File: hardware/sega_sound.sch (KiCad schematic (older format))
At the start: 3 parts

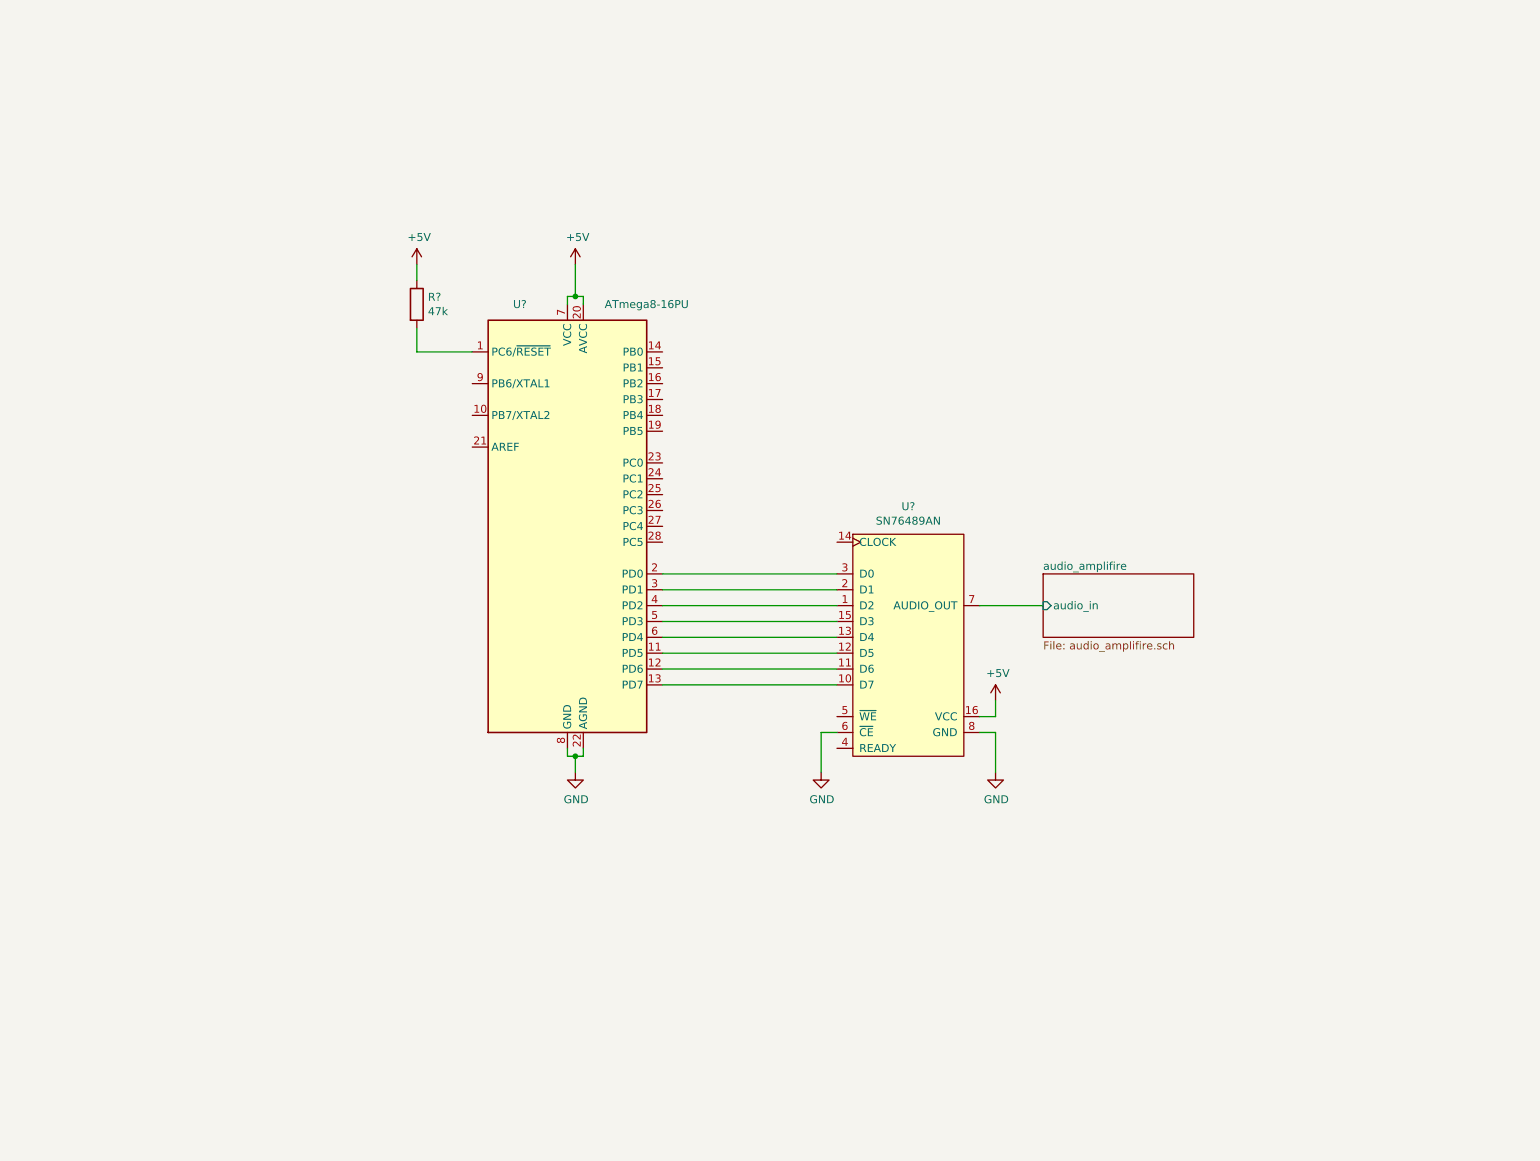
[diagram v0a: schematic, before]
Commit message: changed schematic
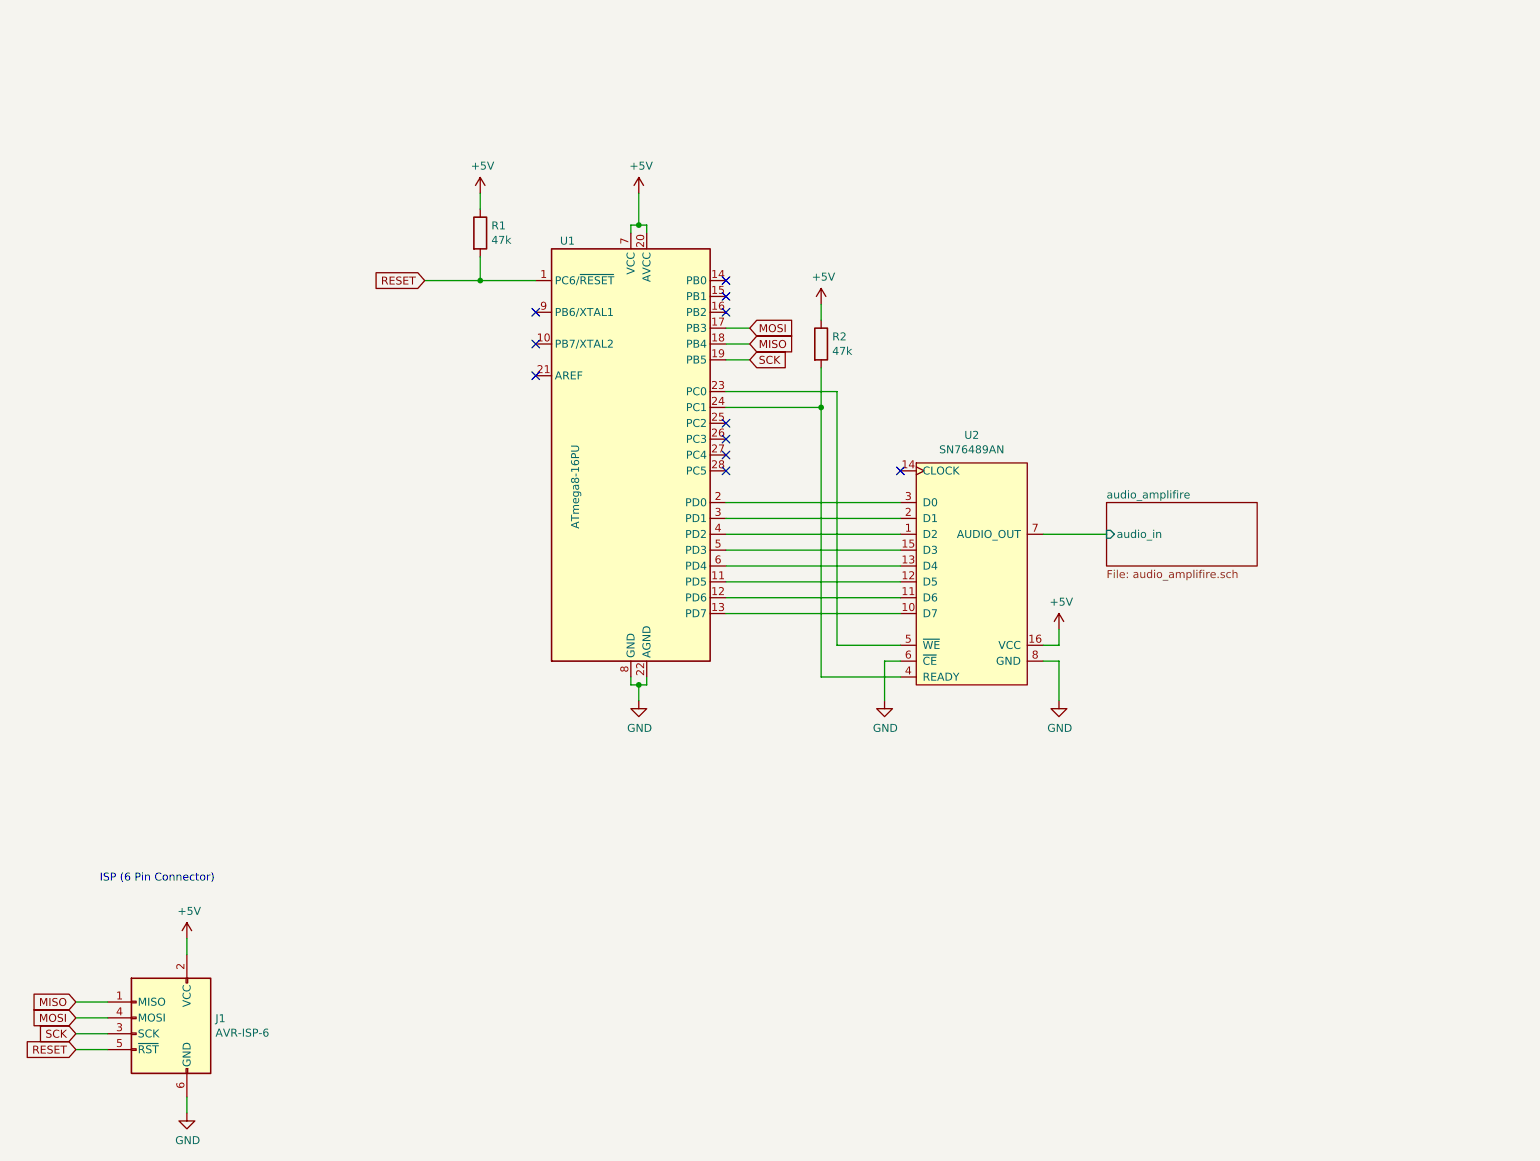
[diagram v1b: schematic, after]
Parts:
- removed U?: ATmega8-16PU, Package_DIP:DIP-28_W7.62mm, symbol MCU_Microchip_ATmega:ATmega8-16PU
- added J1: AVR-ISP-6, symbol Connector:AVR-ISP-6
- added R2: 47k, symbol Device:R
- added U1: ATmega8-16PU, Package_DIP:DIP-28_W7.62mm, symbol MCU_Microchip_ATmega:ATmega8-16PU
- gave numbers to parts that had none: 2
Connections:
- net +5V: now also J1.2 (VCC), R2.1, U1.20 (AVCC), U1.7 (VCC)
- net GND: now also J1.6 (GND), U1.22 (AGND), U1.8 (GND)
- net RESET: now reaches R1.2
- net RESET: now also J1.5 (~RST), U1.1 (PC6/~RESET)
- net at U2.12 (D5): now also U1.11 (PD5)
- net at U2.11 (D6): now also U1.12 (PD6)
- net at U2.10 (D7): now also U1.13 (PD7)
- net at U2.3 (D0): now also U1.2 (PD0)
- net at U2.2 (D1): now also U1.3 (PD1)
- net at U2.1 (D2): now also U1.4 (PD2)
- net at U2.15 (D3): now also U1.5 (PD3)
- net at U2.13 (D4): now also U1.6 (PD4)
- net at U2.4 (READY): now also R2.2, U1.24 (PC1)
- net at U2.5 (~WE): now also U1.23 (PC0)
- new net MISO: J1.1 (MISO), U1.18 (PB4)
- new net MOSI: J1.4 (MOSI), U1.17 (PB3)
- new net SCK: J1.3 (SCK), U1.19 (PB5)
- no-connect marks 0 -> 11
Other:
- note added: "ISP (6 Pin Connector)"
- moved on the sheet: R1, U2

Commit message: removed pullup resistor 47k for READY signal
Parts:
- removed R2: 47k, symbol Device:R
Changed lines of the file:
@@
 $EndDescr
 $Comp
-L power:+5V #PWR04
+L power:+5V #PWR03
 U 1 1 5E271210
 P 7250 4400
-F 0 "#PWR04" H 7250 4250 50  0001 C CNN
+F 0 "#PWR03" H 7250 4250 50  0001 C CNN
 F 1 "+5V" H 7265 4573 50  0000 C CNN
 F 2 "" H 7250 4400 50  0001 C CNN
@@
 Connection ~ 4600 1850
 $Comp
-L power:GND #PWR05
+L power:GND #PWR04
 U 1 1 5E273378
 P 4600 4850
-F 0 "#PWR05" H 4600 4600 50  0001 C CNN
+F 0 "#PWR04" H 4600 4600 50  0001 C CNN
 F 1 "GND" H 4605 4677 50  0000 C CNN
 F 2 "" H 4600 4850 50  0001 C CNN
@@
 Connection ~ 4600 4750
 $Comp
-L power:GND #PWR07
+L power:GND #PWR06
 U 1 1 5E2743A8
 P 7250 4850
-F 0 "#PWR07" H 7250 4600 50  0001 C CNN
+F 0 "#PWR06" H 7250 4600 50  0001 C CNN
 F 1 "GND" H 7255 4677 50  0000 C CNN
 F 2 "" H 7250 4850 50  0001 C CNN
@@
 	7250 4600 7250 4850
 $Comp
-L power:GND #PWR06
+L power:GND #PWR05
 U 1 1 5E275910
 P 6150 4850
-F 0 "#PWR06" H 6150 4600 50  0001 C CNN
+F 0 "#PWR05" H 6150 4600 50  0001 C CNN
 F 1 "GND" H 6155 4677 50  0000 C CNN
 F 2 "" H 6150 4850 50  0001 C CNN
@@
 Connection ~ 3600 2200
 $Comp
-L power:+5V #PWR08
+L power:+5V #PWR07
 U 1 1 5E279685
 P 1750 6350
-F 0 "#PWR08" H 1750 6200 50  0001 C CNN
+F 0 "#PWR07" H 1750 6200 50  0001 C CNN
 F 1 "+5V" H 1765 6523 50  0000 C CNN
 F 2 "" H 1750 6350 50  0001 C CNN
@@
 $EndComp
 $Comp
-L power:GND #PWR09
+L power:GND #PWR08
 U 1 1 5E279E4E
 P 1750 7450
-F 0 "#PWR09" H 1750 7200 50  0001 C CNN
+F 0 "#PWR08" H 1750 7200 50  0001 C CNN
 F 1 "GND" H 1755 7277 50  0000 C CNN
 F 2 "" H 1750 7450 50  0001 C CNN
@@
 NoConn ~ 3950 2400
 NoConn ~ 6250 3400
-$Comp
-L Device:R R2
-U 1 1 5E294E27
-P 5750 2600
-F 0 "R2" H 5820 2646 50  0000 L CNN
-F 1 "47k" H 5820 2555 50  0000 L CNN
-F 2 "" V 5680 2600 50  0001 C CNN
-F 3 "~" H 5750 2600 50  0001 C CNN
-	1    5750 2600
-	1    0    0    -1
-$EndComp
-Wire Wire Line
-	5750 2750 5750 3000
-Connection ~ 5750 3000
-$Comp
-L power:+5V #PWR03
-U 1 1 5E299157
-P 5750 2350
-F 0 "#PWR03" H 5750 2200 50  0001 C CNN
-F 1 "+5V" H 5765 2523 50  0000 C CNN
-F 2 "" H 5750 2350 50  0001 C CNN
-F 3 "" H 5750 2350 50  0001 C CNN
-	1    5750 2350
-	1    0    0    -1
-$EndComp
-Wire Wire Line
-	5750 2350 5750 2450
 $EndSCHEMATC

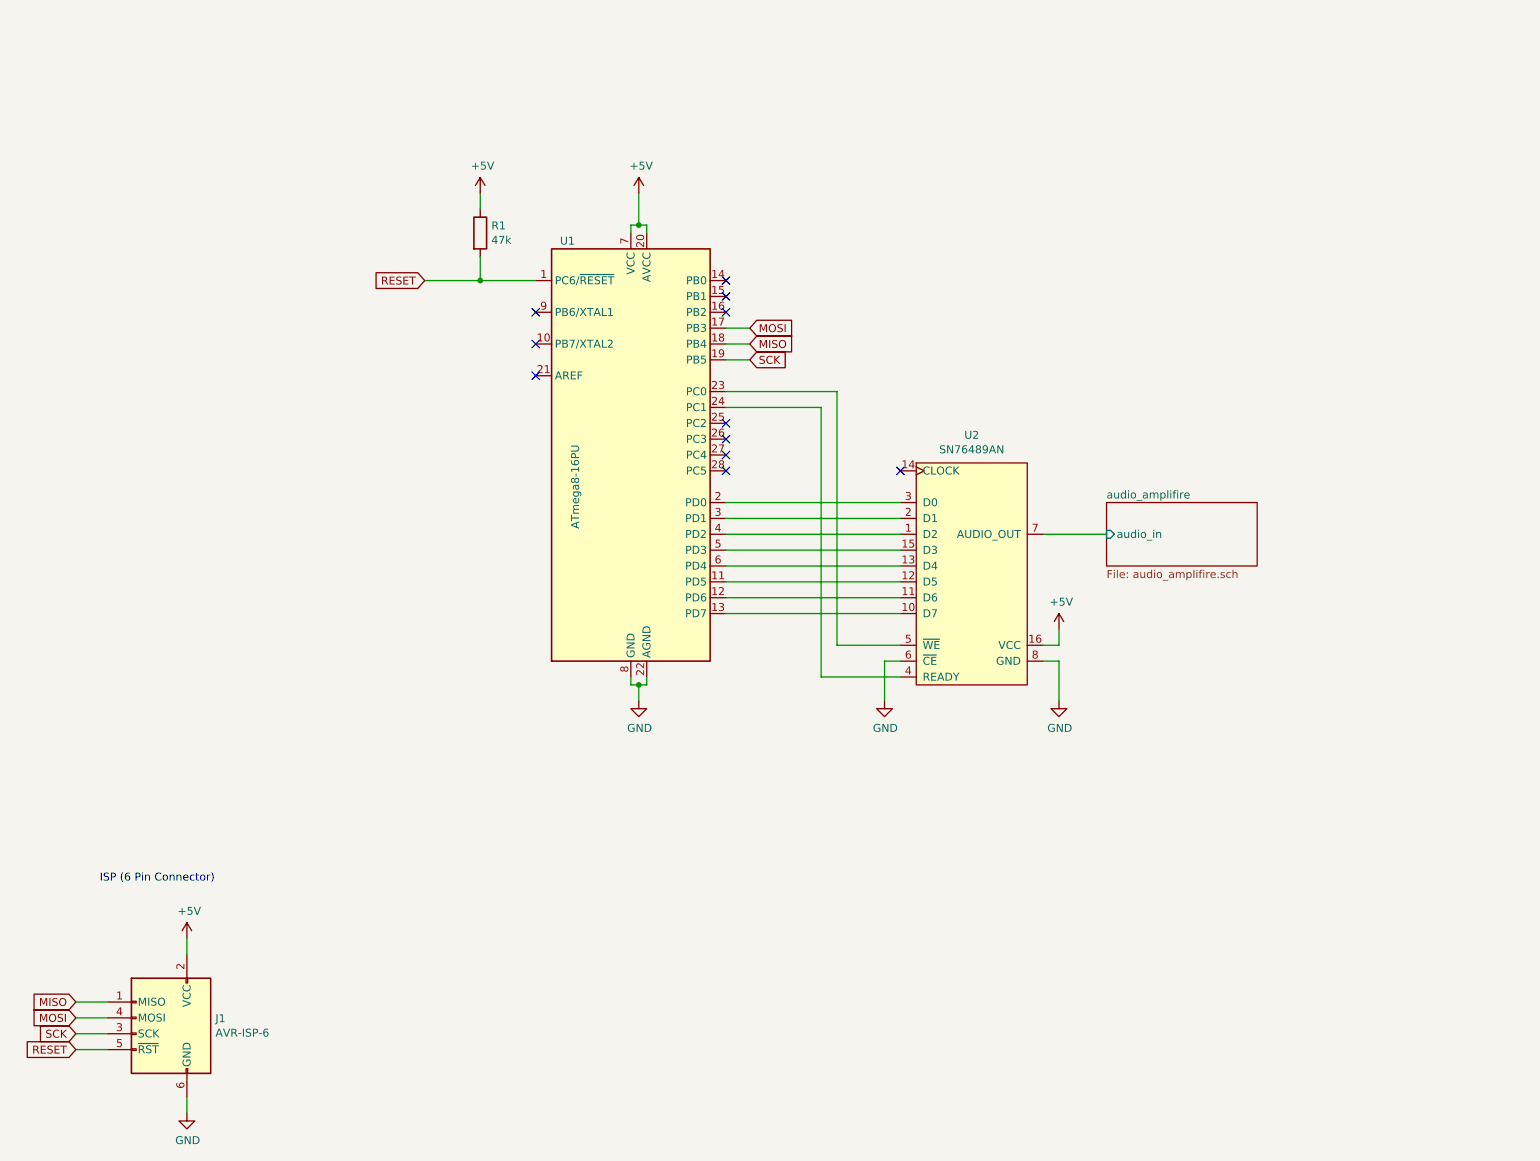
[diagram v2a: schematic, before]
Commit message: changed schematic
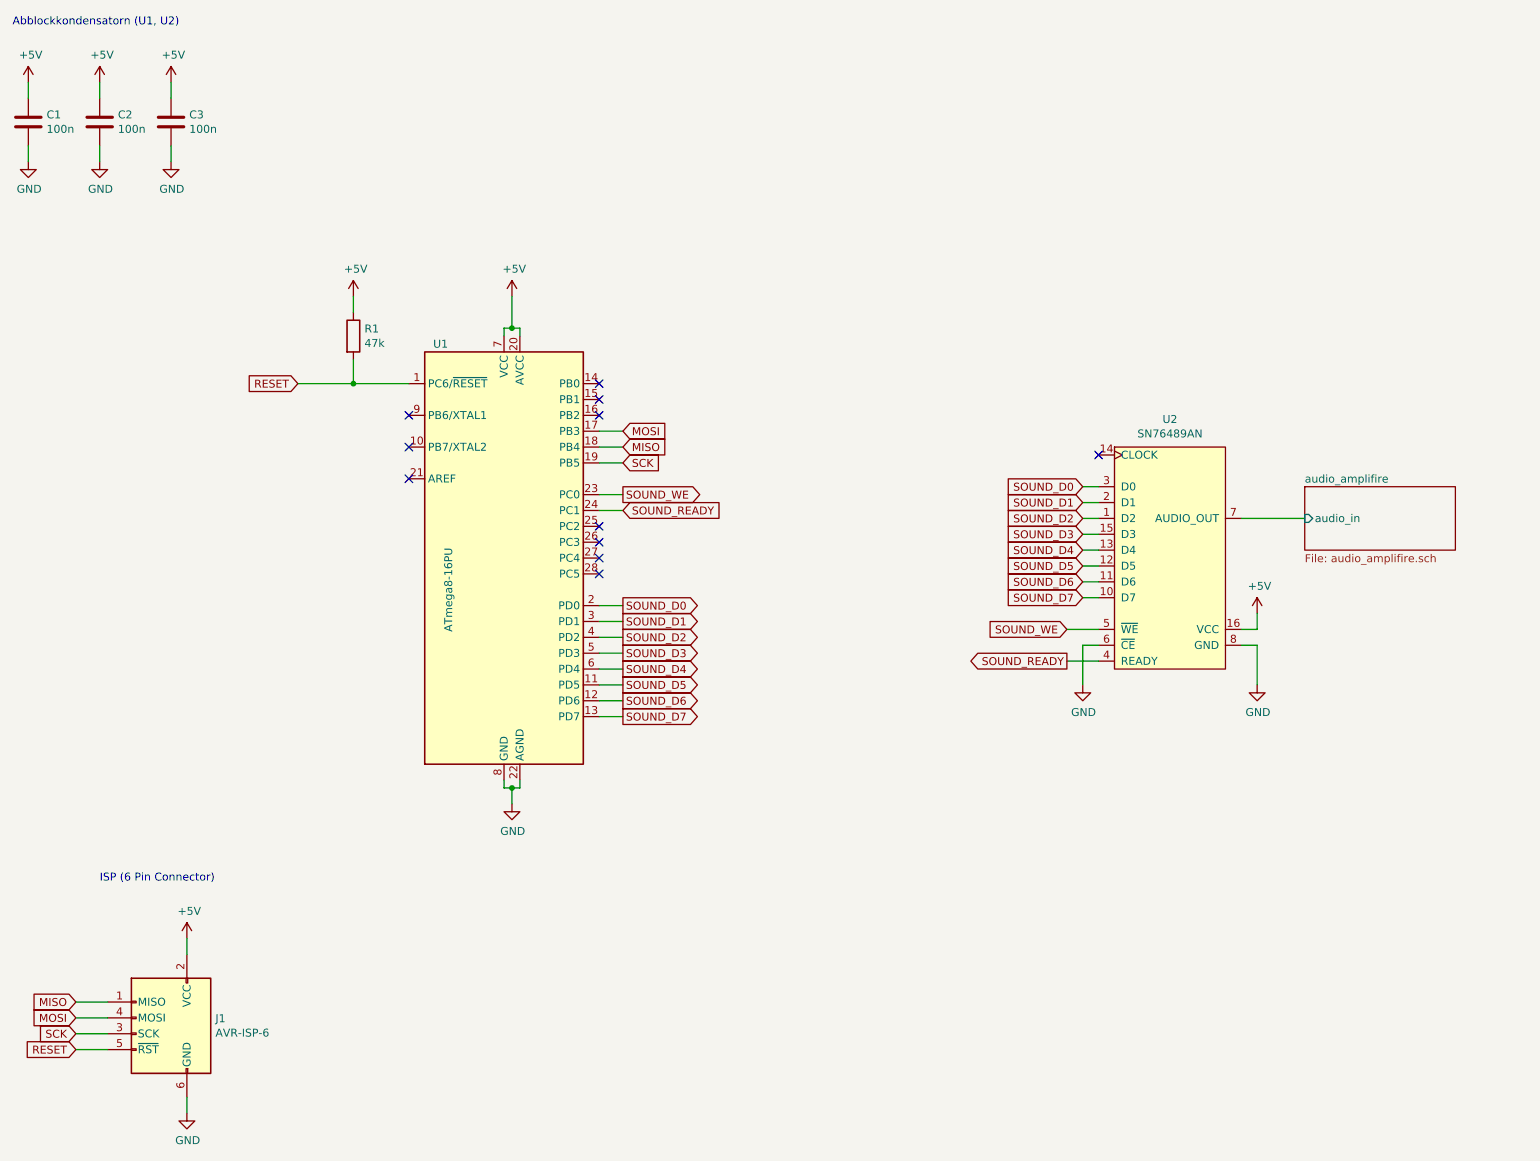
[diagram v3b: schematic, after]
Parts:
- added C1, C2, C3: 100n, symbol Device:C
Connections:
- net +5V: now also C1.1, C2.1, C3.1
- net GND: now also C1.2, C2.2, C3.2
- net SOUND_D2: now reaches U1.4 (PD2), U2.1 (D2)
- net SOUND_D7: now reaches U1.13 (PD7), U2.10 (D7)
- net SOUND_D6: now reaches U1.12 (PD6), U2.11 (D6)
- net SOUND_D5: now reaches U1.11 (PD5), U2.12 (D5)
- net SOUND_D4: now reaches U1.6 (PD4), U2.13 (D4)
- net SOUND_D3: now reaches U1.5 (PD3), U2.15 (D3)
- net SOUND_D1: now reaches U1.3 (PD1), U2.2 (D1)
- net SOUND_D0: now reaches U1.2 (PD0), U2.3 (D0)
- net SOUND_READY: now reaches U1.24 (PC1), U2.4 (READY)
- net SOUND_WE: now reaches U1.23 (PC0), U2.5 (~WE)
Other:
- note added: "Abblockkondensatorn (U1, U2)"
- moved on the sheet: R1, U1

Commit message: added status led in schematic
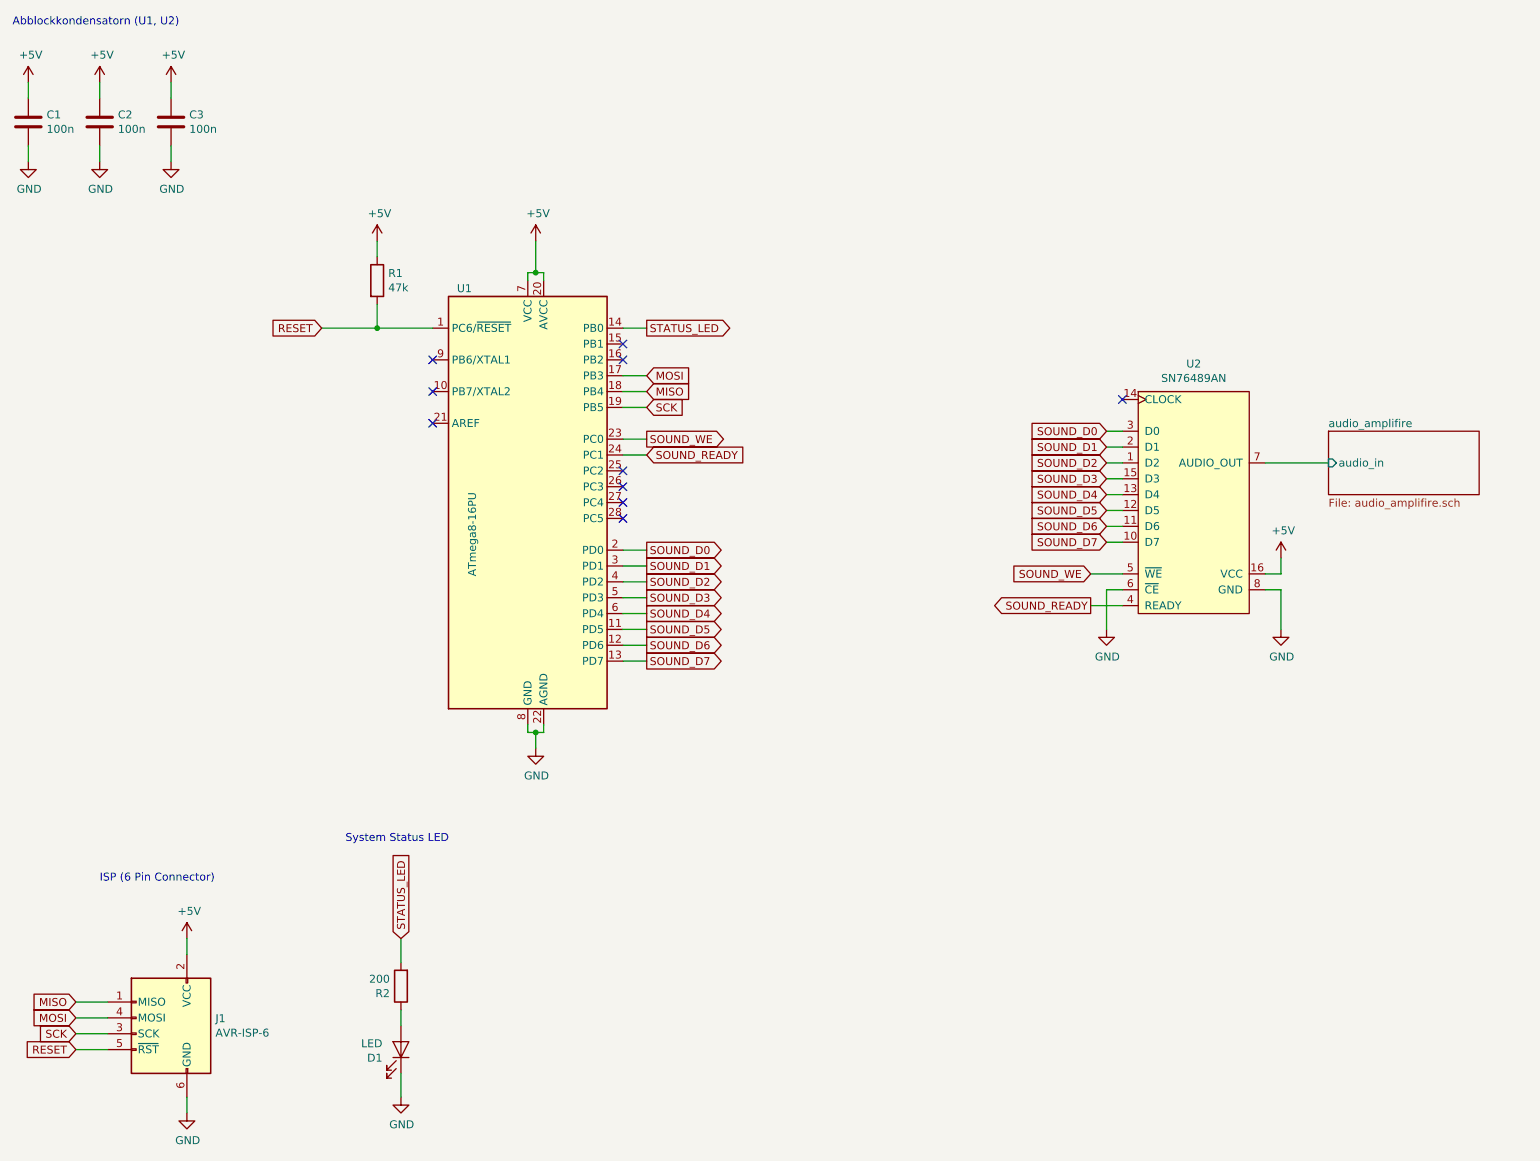
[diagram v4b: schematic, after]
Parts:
- added D1: LED, symbol Device:LED
- added R2: 200, symbol Device:R
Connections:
- net GND: now also D1.1 (K)
- net STATUS_LED: now reaches U1.14 (PB0)
- net STATUS_LED: now also R2.2
- new net: D1.2 (A), R2.1
- no-connect marks 11 -> 10
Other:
- note added: "System Status LED"
- moved on the sheet: R1, U1, U2
